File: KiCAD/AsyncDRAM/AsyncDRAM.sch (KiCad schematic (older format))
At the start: 6 parts

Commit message: Update
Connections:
- net GND: now reaches C1.2
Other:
- moved on the sheet: C1, C2, C3, C4, KM44256_1, KM44256_2
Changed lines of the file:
@@
 EESchema Schematic File Version 4
+LIBS:AsyncDRAM-cache
 EELAYER 30 0
 EELAYER END
@@
 L MyLibrary:KM44C256BP-8 KM44256_1
 U 1 1 5DA9F5FC
-P 4200 2250
-F 0 "KM44256_1" H 4869 2296 50  0000 L CNN
-F 1 "KM44C256BP-8" H 4869 2205 50  0000 L CNN
-F 2 "DIP:DIP-20_W7.62mm" H 4150 2350 50  0001 C CNN
-F 3 "" H 4150 2350 50  0001 C CNN
-	1    4200 2250
+P 1750 3100
+F 0 "KM44256_1" H 2419 3146 50  0000 L CNN
+F 1 "KM44C256BP-8" H 2419 3055 50  0000 L CNN
+F 2 "DIP:DIP-20_W7.62mm" H 1700 3200 50  0001 C CNN
+F 3 "" H 1700 3200 50  0001 C CNN
+	1    1750 3100
 	1    0    0    -1
 $EndComp
@@
 L MyLibrary:KM44C256BP-8 KM44256_2
 U 1 1 5DA9FC1B
-P 4200 3800
-F 0 "KM44256_2" H 4869 3846 50  0000 L CNN
-F 1 "KM44C256BP-8" H 4869 3755 50  0000 L CNN
-F 2 "DIP:DIP-20_W7.62mm" H 4150 3900 50  0001 C CNN
-F 3 "" H 4150 3900 50  0001 C CNN
-	1    4200 3800
+P 3100 3750
+F 0 "KM44256_2" H 3769 3796 50  0000 L CNN
+F 1 "KM44C256BP-8" H 3769 3705 50  0000 L CNN
+F 2 "DIP:DIP-20_W7.62mm" H 3050 3850 50  0001 C CNN
+F 3 "" H 3050 3850 50  0001 C CNN
+	1    3100 3750
 	1    0    0    -1
 $EndComp
@@
 L Device:C C1
 U 1 1 5DAA5148
-P 2850 1950
-F 0 "C1" H 2965 1996 50  0000 L CNN
-F 1 "100nF" H 2965 1905 50  0000 L CNN
-F 2 "CapacitorSMD:C_0805_2012Metric" H 2888 1800 50  0001 C CNN
-F 3 "~" H 2850 1950 50  0001 C CNN
-	1    2850 1950
-	1    0    0    -1
+P 1100 1100
+F 0 "C1" H 1215 1146 50  0000 L CNN
+F 1 "100nF" H 1215 1055 50  0000 L CNN
+F 2 "CapacitorSMD:C_0805_2012Metric" H 1138 950 50  0001 C CNN
+F 3 "~" H 1100 1100 50  0001 C CNN
+	1    1100 1100
+	0    -1   -1   0
 $EndComp
 $Comp
 L Device:C C2
 U 1 1 5DAA556A
-P 2850 2350
-F 0 "C2" H 2965 2396 50  0000 L CNN
-F 1 "100nF" H 2965 2305 50  0000 L CNN
-F 2 "CapacitorSMD:C_0805_2012Metric" H 2888 2200 50  0001 C CNN
-F 3 "~" H 2850 2350 50  0001 C CNN
-	1    2850 2350
-	1    0    0    -1
+P 1100 1300
+F 0 "C2" H 1215 1346 50  0000 L CNN
+F 1 "100nF" H 1215 1255 50  0000 L CNN
+F 2 "CapacitorSMD:C_0805_2012Metric" H 1138 1150 50  0001 C CNN
+F 3 "~" H 1100 1300 50  0001 C CNN
+	1    1100 1300
+	0    1    1    0
 $EndComp
 $Comp
 L Device:C C3
 U 1 1 5DAA5879
-P 2850 2750
-F 0 "C3" H 2965 2796 50  0000 L CNN
-F 1 "47µF" H 2965 2705 50  0000 L CNN
-F 2 "CapacitorSMD:C_0805_2012Metric" H 2888 2600 50  0001 C CNN
-F 3 "~" H 2850 2750 50  0001 C CNN
-	1    2850 2750
-	1    0    0    -1
+P 2000 1100
+F 0 "C3" H 2115 1146 50  0000 L CNN
+F 1 "47µF" H 2115 1055 50  0000 L CNN
+F 2 "CapacitorSMD:C_0805_2012Metric" H 2038 950 50  0001 C CNN
+F 3 "~" H 2000 1100 50  0001 C CNN
+	1    2000 1100
+	0    -1   -1   0
 $EndComp
 $Comp
 L Device:C C4
 U 1 1 5DAA6473
-P 2850 3150
-F 0 "C4" H 2965 3196 50  0000 L CNN
-F 1 "47µF" H 2965 3105 50  0000 L CNN
-F 2 "CapacitorSMD:C_0805_2012Metric" H 2888 3000 50  0001 C CNN
-F 3 "~" H 2850 3150 50  0001 C CNN
-	1    2850 3150
-	1    0    0    -1
+P 2000 1350
+F 0 "C4" H 2115 1396 50  0000 L CNN
+F 1 "47µF" H 2115 1305 50  0000 L CNN
+F 2 "CapacitorSMD:C_0805_2012Metric" H 2038 1200 50  0001 C CNN
+F 3 "~" H 2000 1350 50  0001 C CNN
+	1    2000 1350
+	0    1    1    0
 $EndComp
+$Comp
+L Power:+5V #PWR?
+U 1 1 5DAAB244
+P 850 1100
+F 0 "#PWR?" H 850 950 50  0001 C CNN
+F 1 "+5V" V 865 1228 50  0000 L CNN
+F 2 "" H 850 1100 50  0001 C CNN
+F 3 "" H 850 1100 50  0001 C CNN
+	1    850  1100
+	0    -1   -1   0
+$EndComp
+$Comp
+L Power:GND #PWR?
+U 1 1 5DAAB9E6
+P 1350 1100
+F 0 "#PWR?" H 1350 850 50  0001 C CNN
+F 1 "GND" V 1355 972 50  0000 R CNN
+F 2 "" H 1350 1100 50  0001 C CNN
+F 3 "" H 1350 1100 50  0001 C CNN
+	1    1350 1100
+	0    -1   -1   0
+$EndComp
+Wire Wire Line
+	1250 1100 1350 1100
 $EndSCHEMATC

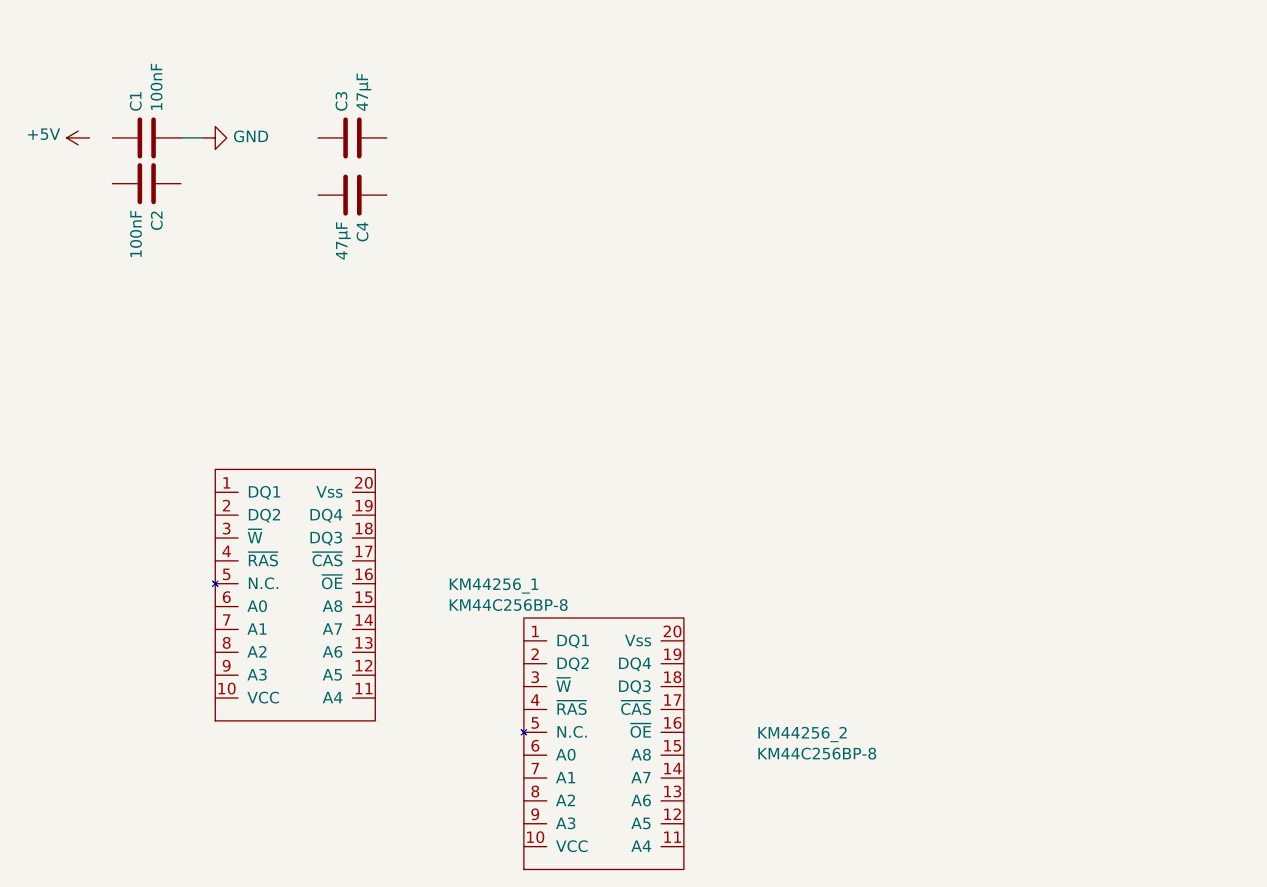
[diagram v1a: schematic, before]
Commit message: Added Datasheet for possible µC, added QFP Footprints
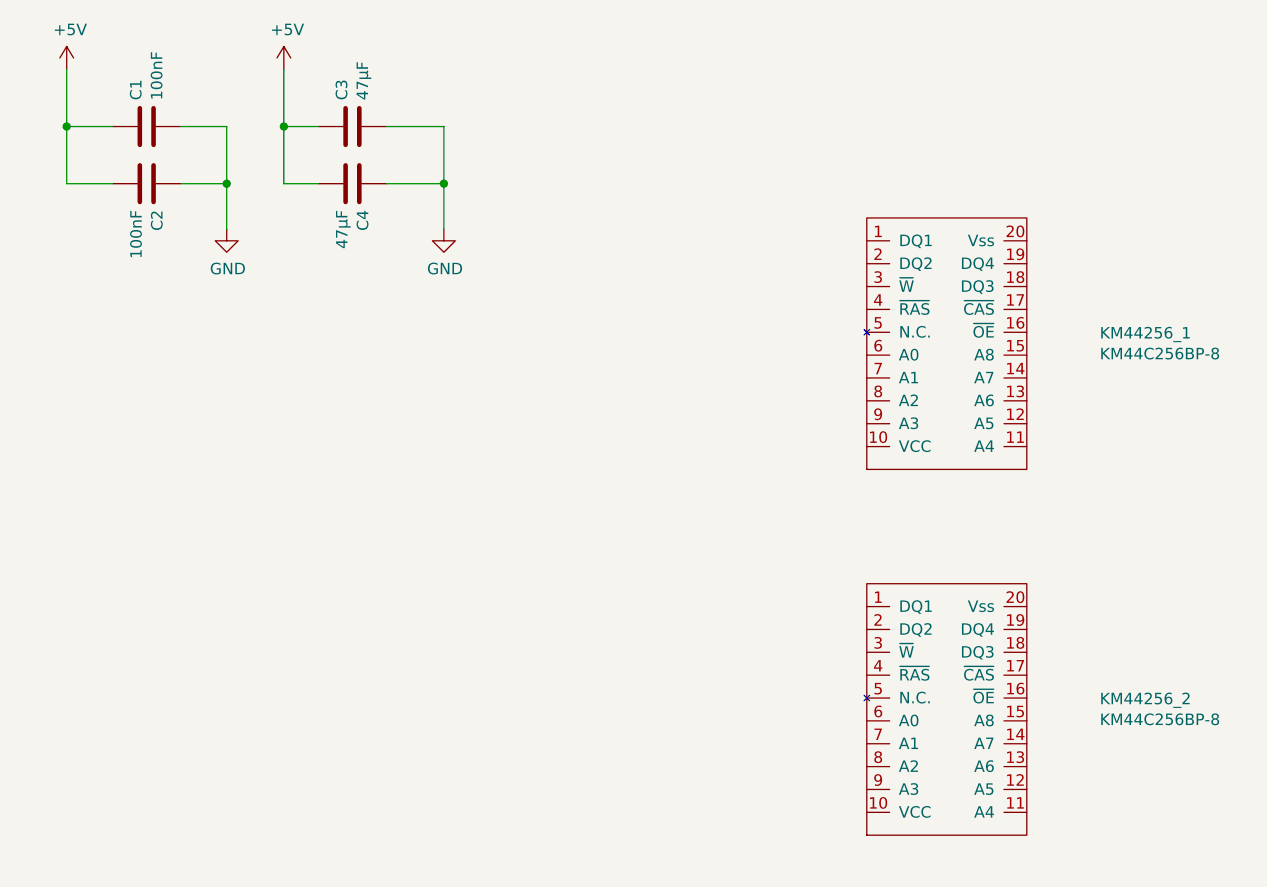
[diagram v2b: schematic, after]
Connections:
- net +5V: now also C1.1, C2.2, C3.1, C4.2
- net GND: now also C2.1, C3.2, C4.1
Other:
- moved on the sheet: C1, C3, C4, KM44256_1, KM44256_2
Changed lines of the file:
@@
 L MyLibrary:KM44C256BP-8 KM44256_1
 U 1 1 5DA9F5FC
-P 1750 3100
-F 0 "KM44256_1" H 2419 3146 50  0000 L CNN
-F 1 "KM44C256BP-8" H 2419 3055 50  0000 L CNN
-F 2 "DIP:DIP-20_W7.62mm" H 1700 3200 50  0001 C CNN
-F 3 "" H 1700 3200 50  0001 C CNN
-	1    1750 3100
+P 4600 2000
+F 0 "KM44256_1" H 5269 2046 50  0000 L CNN
+F 1 "KM44C256BP-8" H 5269 1955 50  0000 L CNN
+F 2 "DIP:DIP-20_W7.62mm" H 4550 2100 50  0001 C CNN
+F 3 "" H 4550 2100 50  0001 C CNN
+	1    4600 2000
 	1    0    0    -1
 $EndComp
@@
 L MyLibrary:KM44C256BP-8 KM44256_2
 U 1 1 5DA9FC1B
-P 3100 3750
-F 0 "KM44256_2" H 3769 3796 50  0000 L CNN
-F 1 "KM44C256BP-8" H 3769 3705 50  0000 L CNN
-F 2 "DIP:DIP-20_W7.62mm" H 3050 3850 50  0001 C CNN
-F 3 "" H 3050 3850 50  0001 C CNN
-	1    3100 3750
+P 4600 3600
+F 0 "KM44256_2" H 5269 3646 50  0000 L CNN
+F 1 "KM44C256BP-8" H 5269 3555 50  0000 L CNN
+F 2 "DIP:DIP-20_W7.62mm" H 4550 3700 50  0001 C CNN
+F 3 "" H 4550 3700 50  0001 C CNN
+	1    4600 3600
 	1    0    0    -1
 $EndComp
@@
 L Device:C C1
 U 1 1 5DAA5148
-P 1100 1100
-F 0 "C1" H 1215 1146 50  0000 L CNN
-F 1 "100nF" H 1215 1055 50  0000 L CNN
-F 2 "CapacitorSMD:C_0805_2012Metric" H 1138 950 50  0001 C CNN
-F 3 "~" H 1100 1100 50  0001 C CNN
-	1    1100 1100
+P 1100 1050
+F 0 "C1" H 1215 1096 50  0000 L CNN
+F 1 "100nF" H 1215 1005 50  0000 L CNN
+F 2 "CapacitorSMD:C_0805_2012Metric" H 1138 900 50  0001 C CNN
+F 3 "~" H 1100 1050 50  0001 C CNN
+	1    1100 1050
 	0    -1   -1   0
 $EndComp
@@
 L Device:C C3
 U 1 1 5DAA5879
-P 2000 1100
-F 0 "C3" H 2115 1146 50  0000 L CNN
-F 1 "47µF" H 2115 1055 50  0000 L CNN
-F 2 "CapacitorSMD:C_0805_2012Metric" H 2038 950 50  0001 C CNN
-F 3 "~" H 2000 1100 50  0001 C CNN
-	1    2000 1100
+P 2000 1050
+F 0 "C3" H 2115 1096 50  0000 L CNN
+F 1 "47µF" H 2115 1005 50  0000 L CNN
+F 2 "CapacitorSMD:C_0805_2012Metric" H 2038 900 50  0001 C CNN
+F 3 "~" H 2000 1050 50  0001 C CNN
+	1    2000 1050
 	0    -1   -1   0
 $EndComp
@@
 L Device:C C4
 U 1 1 5DAA6473
-P 2000 1350
-F 0 "C4" H 2115 1396 50  0000 L CNN
-F 1 "47µF" H 2115 1305 50  0000 L CNN
-F 2 "CapacitorSMD:C_0805_2012Metric" H 2038 1200 50  0001 C CNN
-F 3 "~" H 2000 1350 50  0001 C CNN
-	1    2000 1350
+P 2000 1300
+F 0 "C4" H 2115 1346 50  0000 L CNN
+F 1 "47µF" H 2115 1255 50  0000 L CNN
+F 2 "CapacitorSMD:C_0805_2012Metric" H 2038 1150 50  0001 C CNN
+F 3 "~" H 2000 1300 50  0001 C CNN
+	1    2000 1300
 	0    1    1    0
 $EndComp
@@
 L Power:+5V #PWR?
 U 1 1 5DAAB244
-P 850 1100
-F 0 "#PWR?" H 850 950 50  0001 C CNN
-F 1 "+5V" V 865 1228 50  0000 L CNN
-F 2 "" H 850 1100 50  0001 C CNN
-F 3 "" H 850 1100 50  0001 C CNN
-	1    850  1100
-	0    -1   -1   0
+P 750 800
+F 0 "#PWR?" H 750 650 50  0001 C CNN
+F 1 "+5V" H 765 973 50  0000 C CNN
+F 2 "" H 750 800 50  0001 C CNN
+F 3 "" H 750 800 50  0001 C CNN
+	1    750  800
+	1    0    0    -1
+$EndComp
+$Comp
+L Power:+5V #PWR?
+U 1 1 5DAB814C
+P 1700 800
+F 0 "#PWR?" H 1700 650 50  0001 C CNN
+F 1 "+5V" H 1715 973 50  0000 C CNN
+F 2 "" H 1700 800 50  0001 C CNN
+F 3 "" H 1700 800 50  0001 C CNN
+	1    1700 800
+	1    0    0    -1
 $EndComp
 $Comp
 L Power:GND #PWR?
-U 1 1 5DAAB9E6
-P 1350 1100
-F 0 "#PWR?" H 1350 850 50  0001 C CNN
-F 1 "GND" V 1355 972 50  0000 R CNN
-F 2 "" H 1350 1100 50  0001 C CNN
-F 3 "" H 1350 1100 50  0001 C CNN
-	1    1350 1100
-	0    -1   -1   0
+U 1 1 5DAB9C68
+P 1450 1500
+F 0 "#PWR?" H 1450 1250 50  0001 C CNN
+F 1 "GND" H 1455 1327 50  0000 C CNN
+F 2 "" H 1450 1500 50  0001 C CNN
+F 3 "" H 1450 1500 50  0001 C CNN
+	1    1450 1500
+	1    0    0    -1
 $EndComp
 Wire Wire Line
-	1250 1100 1350 1100
+	950  1050 750  1050
+Wire Wire Line
+	750  1050 750  800
+Wire Wire Line
+	950  1300 750  1300
+Wire Wire Line
+	750  1300 750  1050
+Connection ~ 750  1050
+Wire Wire Line
+	1850 1050 1700 1050
+Wire Wire Line
+	1700 800  1700 1050
+Wire Wire Line
+	1250 1300 1450 1300
+Wire Wire Line
+	1250 1050 1450 1050
+Wire Wire Line
+	1450 1050 1450 1300
+Connection ~ 1450 1300
+Wire Wire Line
+	1450 1300 1450 1500
+$Comp
+L Power:GND #PWR?
+U 1 1 5DABDCDA
+P 2400 1500
+F 0 "#PWR?" H 2400 1250 50  0001 C CNN
+F 1 "GND" H 2405 1327 50  0000 C CNN
+F 2 "" H 2400 1500 50  0001 C CNN
+F 3 "" H 2400 1500 50  0001 C CNN
+	1    2400 1500
+	1    0    0    -1
+$EndComp
+Wire Wire Line
+	2150 1050 2400 1050
+Wire Wire Line
+	2400 1050 2400 1300
+Wire Wire Line
+	2150 1300 2400 1300
+Connection ~ 2400 1300
+Wire Wire Line
+	2400 1300 2400 1500
+Wire Wire Line
+	1850 1300 1700 1300
+Wire Wire Line
+	1700 1300 1700 1050
+Connection ~ 1700 1050
 $EndSCHEMATC

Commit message: First Commit from ArchLinux Tablet
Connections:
- net +5V: now also KM44256_1.10 (VCC), KM44256_2.10 (VCC)
- net GND: now also KM44256_1.20 (Vss), KM44256_2.20 (Vss)
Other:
- moved on the sheet: KM44256_2
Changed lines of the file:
@@
 $EndDescr
-$Comp
-L MyLibrary:KM44C256BP-8 KM44256_1
-U 1 1 5DA9F5FC
-P 4600 2000
-F 0 "KM44256_1" H 5269 2046 50  0000 L CNN
-F 1 "KM44C256BP-8" H 5269 1955 50  0000 L CNN
-F 2 "DIP:DIP-20_W7.62mm" H 4550 2100 50  0001 C CNN
-F 3 "" H 4550 2100 50  0001 C CNN
-	1    4600 2000
-	1    0    0    -1
-$EndComp
 $Comp
 L MyLibrary:KM44C256BP-8 KM44256_2
 U 1 1 5DA9FC1B
-P 4600 3600
-F 0 "KM44256_2" H 5269 3646 50  0000 L CNN
-F 1 "KM44C256BP-8" H 5269 3555 50  0000 L CNN
-F 2 "DIP:DIP-20_W7.62mm" H 4550 3700 50  0001 C CNN
-F 3 "" H 4550 3700 50  0001 C CNN
-	1    4600 3600
+P 4600 3350
+F 0 "KM44256_2" H 5269 3396 50  0000 L CNN
+F 1 "KM44C256BP-8" H 5269 3305 50  0000 L CNN
+F 2 "DIP:DIP-20_W7.62mm" H 4550 3450 50  0001 C CNN
+F 3 "" H 4550 3450 50  0001 C CNN
+	1    4600 3350
 	1    0    0    -1
 $EndComp
@@
 $EndComp
 $Comp
-L Power:+5V #PWR?
-U 1 1 5DAAB244
-P 750 800
-F 0 "#PWR?" H 750 650 50  0001 C CNN
-F 1 "+5V" H 765 973 50  0000 C CNN
-F 2 "" H 750 800 50  0001 C CNN
-F 3 "" H 750 800 50  0001 C CNN
-	1    750  800
-	1    0    0    -1
-$EndComp
-$Comp
-L Power:+5V #PWR?
-U 1 1 5DAB814C
-P 1700 800
-F 0 "#PWR?" H 1700 650 50  0001 C CNN
-F 1 "+5V" H 1715 973 50  0000 C CNN
-F 2 "" H 1700 800 50  0001 C CNN
-F 3 "" H 1700 800 50  0001 C CNN
-	1    1700 800
-	1    0    0    -1
-$EndComp
-$Comp
-L Power:GND #PWR?
-U 1 1 5DAB9C68
-P 1450 1500
-F 0 "#PWR?" H 1450 1250 50  0001 C CNN
-F 1 "GND" H 1455 1327 50  0000 C CNN
-F 2 "" H 1450 1500 50  0001 C CNN
-F 3 "" H 1450 1500 50  0001 C CNN
-	1    1450 1500
-	1    0    0    -1
-$EndComp
+L MyLibrary:KM44C256BP-8 KM44256_1
+U 1 1 5DA9F5FC
+P 4600 2000
+F 0 "KM44256_1" H 4400 2600 50  0000 L CNN
+F 1 "KM44C256BP-8" H 4300 1400 50  0000 L CNN
+F 2 "DIP:DIP-20_W7.62mm" H 4550 2100 50  0001 C CNN
+F 3 "" H 4550 2100 50  0001 C CNN
+	1    4600 2000
+	1    0    0    -1
+$EndComp
+$Comp
+L power:+5V #PWR?
+U 1 1 5DAAB4BD
+P 750 850
+F 0 "#PWR?" H 750 700 50  0001 C CNN
+F 1 "+5V" H 765 1023 50  0000 C CNN
+F 2 "" H 750 850 50  0001 C CNN
+F 3 "" H 750 850 50  0001 C CNN
+	1    750  850
+	1    0    0    -1
+$EndComp
+$Comp
+L power:+5V #PWR?
+U 1 1 5DAAB973
+P 1700 850
+F 0 "#PWR?" H 1700 700 50  0001 C CNN
+F 1 "+5V" H 1715 1023 50  0000 C CNN
+F 2 "" H 1700 850 50  0001 C CNN
+F 3 "" H 1700 850 50  0001 C CNN
+	1    1700 850
+	1    0    0    -1
+$EndComp
+Wire Wire Line
+	1850 1050 1700 1050
+Wire Wire Line
+	1700 1050 1700 850
+Wire Wire Line
+	1850 1300 1700 1300
+Wire Wire Line
+	1700 1300 1700 1050
+Connection ~ 1700 1050
 Wire Wire Line
 	950  1050 750  1050
 Wire Wire Line
-	750  1050 750  800
+	750  1050 750  850
 Wire Wire Line
 	950  1300 750  1300
@@
 	750  1300 750  1050
 Connection ~ 750  1050
-Wire Wire Line
-	1850 1050 1700 1050
-Wire Wire Line
-	1700 800  1700 1050
-Wire Wire Line
-	1250 1300 1450 1300
-Wire Wire Line
-	1250 1050 1450 1050
-Wire Wire Line
-	1450 1050 1450 1300
-Connection ~ 1450 1300
-Wire Wire Line
-	1450 1300 1450 1500
-$Comp
-L Power:GND #PWR?
-U 1 1 5DABDCDA
-P 2400 1500
-F 0 "#PWR?" H 2400 1250 50  0001 C CNN
-F 1 "GND" H 2405 1327 50  0000 C CNN
-F 2 "" H 2400 1500 50  0001 C CNN
-F 3 "" H 2400 1500 50  0001 C CNN
-	1    2400 1500
-	1    0    0    -1
-$EndComp
-Wire Wire Line
-	2150 1050 2400 1050
-Wire Wire Line
-	2400 1050 2400 1300
-Wire Wire Line
-	2150 1300 2400 1300
-Connection ~ 2400 1300
-Wire Wire Line
-	2400 1300 2400 1500
-Wire Wire Line
-	1850 1300 1700 1300
-Wire Wire Line
-	1700 1300 1700 1050
-Connection ~ 1700 1050
+$Comp
+L power:GND #PWR?
+U 1 1 5DAAC339
+P 2350 1550
+F 0 "#PWR?" H 2350 1300 50  0001 C CNN
+F 1 "GND" H 2355 1377 50  0000 C CNN
+F 2 "" H 2350 1550 50  0001 C CNN
+F 3 "" H 2350 1550 50  0001 C CNN
+	1    2350 1550
+	1    0    0    -1
+$EndComp
+$Comp
+L power:GND #PWR?
+U 1 1 5DAAD555
+P 1500 1550
+F 0 "#PWR?" H 1500 1300 50  0001 C CNN
+F 1 "GND" H 1505 1377 50  0000 C CNN
+F 2 "" H 1500 1550 50  0001 C CNN
+F 3 "" H 1500 1550 50  0001 C CNN
+	1    1500 1550
+	1    0    0    -1
+$EndComp
+Wire Wire Line
+	1250 1300 1500 1300
+Wire Wire Line
+	1250 1050 1500 1050
+Wire Wire Line
+	1500 1050 1500 1300
+Connection ~ 1500 1300
+Wire Wire Line
+	1500 1300 1500 1550
+Wire Wire Line
+	2150 1050 2350 1050
+Wire Wire Line
+	2150 1300 2350 1300
+Wire Wire Line
+	2350 1050 2350 1300
+Connection ~ 2350 1300
+Wire Wire Line
+	2350 1300 2350 1550
+$Comp
+L power:+5V #PWR?
+U 1 1 5DAAF45B
+P 4100 2450
+F 0 "#PWR?" H 4100 2300 50  0001 C CNN
+F 1 "+5V" V 4115 2578 50  0000 L CNN
+F 2 "" H 4100 2450 50  0001 C CNN
+F 3 "" H 4100 2450 50  0001 C CNN
+	1    4100 2450
+	0    -1   -1   0
+$EndComp
+Wire Wire Line
+	4100 2450 4250 2450
+$Comp
+L power:GND #PWR?
+U 1 1 5DAAFE76
+P 5300 1500
+F 0 "#PWR?" H 5300 1250 50  0001 C CNN
+F 1 "GND" H 5305 1327 50  0000 C CNN
+F 2 "" H 5300 1500 50  0001 C CNN
+F 3 "" H 5300 1500 50  0001 C CNN
+	1    5300 1500
+	-1   0    0    1
+$EndComp
+Wire Wire Line
+	4950 1550 5300 1550
+Wire Wire Line
+	5300 1550 5300 1500
+$Comp
+L power:+5V #PWR?
+U 1 1 5DAB1081
+P 4100 3800
+F 0 "#PWR?" H 4100 3650 50  0001 C CNN
+F 1 "+5V" V 4115 3928 50  0000 L CNN
+F 2 "" H 4100 3800 50  0001 C CNN
+F 3 "" H 4100 3800 50  0001 C CNN
+	1    4100 3800
+	0    -1   -1   0
+$EndComp
+Wire Wire Line
+	4250 3800 4100 3800
+$Comp
+L power:GND #PWR?
+U 1 1 5DAB36DC
+P 5350 2850
+F 0 "#PWR?" H 5350 2600 50  0001 C CNN
+F 1 "GND" H 5355 2677 50  0000 C CNN
+F 2 "" H 5350 2850 50  0001 C CNN
+F 3 "" H 5350 2850 50  0001 C CNN
+	1    5350 2850
+	-1   0    0    1
+$EndComp
+Wire Wire Line
+	4950 2900 5350 2900
+Wire Wire Line
+	5350 2900 5350 2850
 $EndSCHEMATC

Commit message: Relinked symbols
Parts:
- C1, C2, C3: footprint CapacitorSMD:C_0805_2012Metric -> (none)
- C3: renamed from C4; footprint CapacitorSMD:C_0805_2012Metric -> (none)
- KM44256: renamed from KM44256_1; footprint DIP:DIP-20_W7.62mm -> (none)
- KM44256: renamed from KM44256_2; footprint DIP:DIP-20_W7.62mm -> (none)
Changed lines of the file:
@@
 $EndDescr
 $Comp
-L MyLibrary:KM44C256BP-8 KM44256_2
+L MyLibrary:KM44C256BP-8 KM44256
 U 1 1 5DA9FC1B
 P 4600 3350
-F 0 "KM44256_2" H 5269 3396 50  0000 L CNN
-F 1 "KM44C256BP-8" H 5269 3305 50  0000 L CNN
-F 2 "DIP:DIP-20_W7.62mm" H 4550 3450 50  0001 C CNN
+F 0 "KM44256" H 4600 3950 50  0000 C CNN
+F 1 "KM44C256BP-8" H 4600 2750 50  0000 C CNN
+F 2 "" H 4550 3450 50  0001 C CNN
 F 3 "" H 4550 3450 50  0001 C CNN
 	1    4600 3350
@@
 U 1 1 5DAA5148
 P 1100 1050
-F 0 "C1" H 1215 1096 50  0000 L CNN
-F 1 "100nF" H 1215 1005 50  0000 L CNN
-F 2 "CapacitorSMD:C_0805_2012Metric" H 1138 900 50  0001 C CNN
+F 0 "C1" H 1125 1150 50  0000 L CNN
+F 1 "100nF" H 1125 950 50  0000 L CNN
+F 2 "" H 1138 900 50  0001 C CNN
 F 3 "~" H 1100 1050 50  0001 C CNN
 	1    1100 1050
@@
 U 1 1 5DAA556A
 P 1100 1300
-F 0 "C2" H 1215 1346 50  0000 L CNN
-F 1 "100nF" H 1215 1255 50  0000 L CNN
-F 2 "CapacitorSMD:C_0805_2012Metric" H 1138 1150 50  0001 C CNN
+F 0 "C2" H 1125 1400 50  0000 L CNN
+F 1 "100nF" H 1125 1200 50  0000 L CNN
+F 2 "" H 1138 1150 50  0001 C CNN
 F 3 "~" H 1100 1300 50  0001 C CNN
 	1    1100 1300
@@
 U 1 1 5DAA5879
 P 2000 1050
-F 0 "C3" H 2115 1096 50  0000 L CNN
-F 1 "47µF" H 2115 1005 50  0000 L CNN
-F 2 "CapacitorSMD:C_0805_2012Metric" H 2038 900 50  0001 C CNN
+F 0 "C3" H 2025 1150 50  0000 L CNN
+F 1 "47µF" H 2025 950 50  0000 L CNN
+F 2 "" H 2038 900 50  0001 C CNN
 F 3 "~" H 2000 1050 50  0001 C CNN
 	1    2000 1050
@@
 $EndComp
 $Comp
-L Device:C C4
+L Device:C C3
 U 1 1 5DAA6473
 P 2000 1300
-F 0 "C4" H 2115 1346 50  0000 L CNN
-F 1 "47µF" H 2115 1255 50  0000 L CNN
-F 2 "CapacitorSMD:C_0805_2012Metric" H 2038 1150 50  0001 C CNN
+F 0 "C3" H 2025 1400 50  0000 L CNN
+F 1 "47µF" H 2025 1200 50  0000 L CNN
+F 2 "" H 2038 1150 50  0001 C CNN
 F 3 "~" H 2000 1300 50  0001 C CNN
 	1    2000 1300
@@
 $EndComp
 $Comp
-L MyLibrary:KM44C256BP-8 KM44256_1
+L MyLibrary:KM44C256BP-8 KM44256
 U 1 1 5DA9F5FC
 P 4600 2000
-F 0 "KM44256_1" H 4400 2600 50  0000 L CNN
-F 1 "KM44C256BP-8" H 4300 1400 50  0000 L CNN
-F 2 "DIP:DIP-20_W7.62mm" H 4550 2100 50  0001 C CNN
+F 0 "KM44256" H 4600 2600 50  0000 C CNN
+F 1 "KM44C256BP-8" H 4600 1400 50  0000 C CNN
+F 2 "" H 4550 2100 50  0001 C CNN
 F 3 "" H 4550 2100 50  0001 C CNN
 	1    4600 2000
@@
 $EndComp
 $Comp
-L power:+5V #PWR?
+L Power:+5V #PWR?
 U 1 1 5DAAB4BD
 P 750 850
@@
 $EndComp
 $Comp
-L power:+5V #PWR?
+L Power:+5V #PWR?
 U 1 1 5DAAB973
 P 1700 850
@@
 Connection ~ 750  1050
 $Comp
-L power:GND #PWR?
+L Power:GND #PWR?
 U 1 1 5DAAC339
 P 2350 1550
@@
 $EndComp
 $Comp
-L power:GND #PWR?
+L Power:GND #PWR?
 U 1 1 5DAAD555
 P 1500 1550
@@
 	2350 1300 2350 1550
 $Comp
-L power:+5V #PWR?
+L Power:+5V #PWR?
 U 1 1 5DAAF45B
 P 4100 2450
@@
 	4100 2450 4250 2450
 $Comp
-L power:GND #PWR?
+L Power:GND #PWR?
 U 1 1 5DAAFE76
 P 5300 1500
@@
 	5300 1550 5300 1500
 $Comp
-L power:+5V #PWR?
+L Power:+5V #PWR?
 U 1 1 5DAB1081
 P 4100 3800
@@
 	4250 3800 4100 3800
 $Comp
-L power:GND #PWR?
+L Power:GND #PWR?
 U 1 1 5DAB36DC
 P 5350 2850
